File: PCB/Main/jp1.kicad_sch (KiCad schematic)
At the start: 1 part, among them U1 ORANGE_PI_CM4

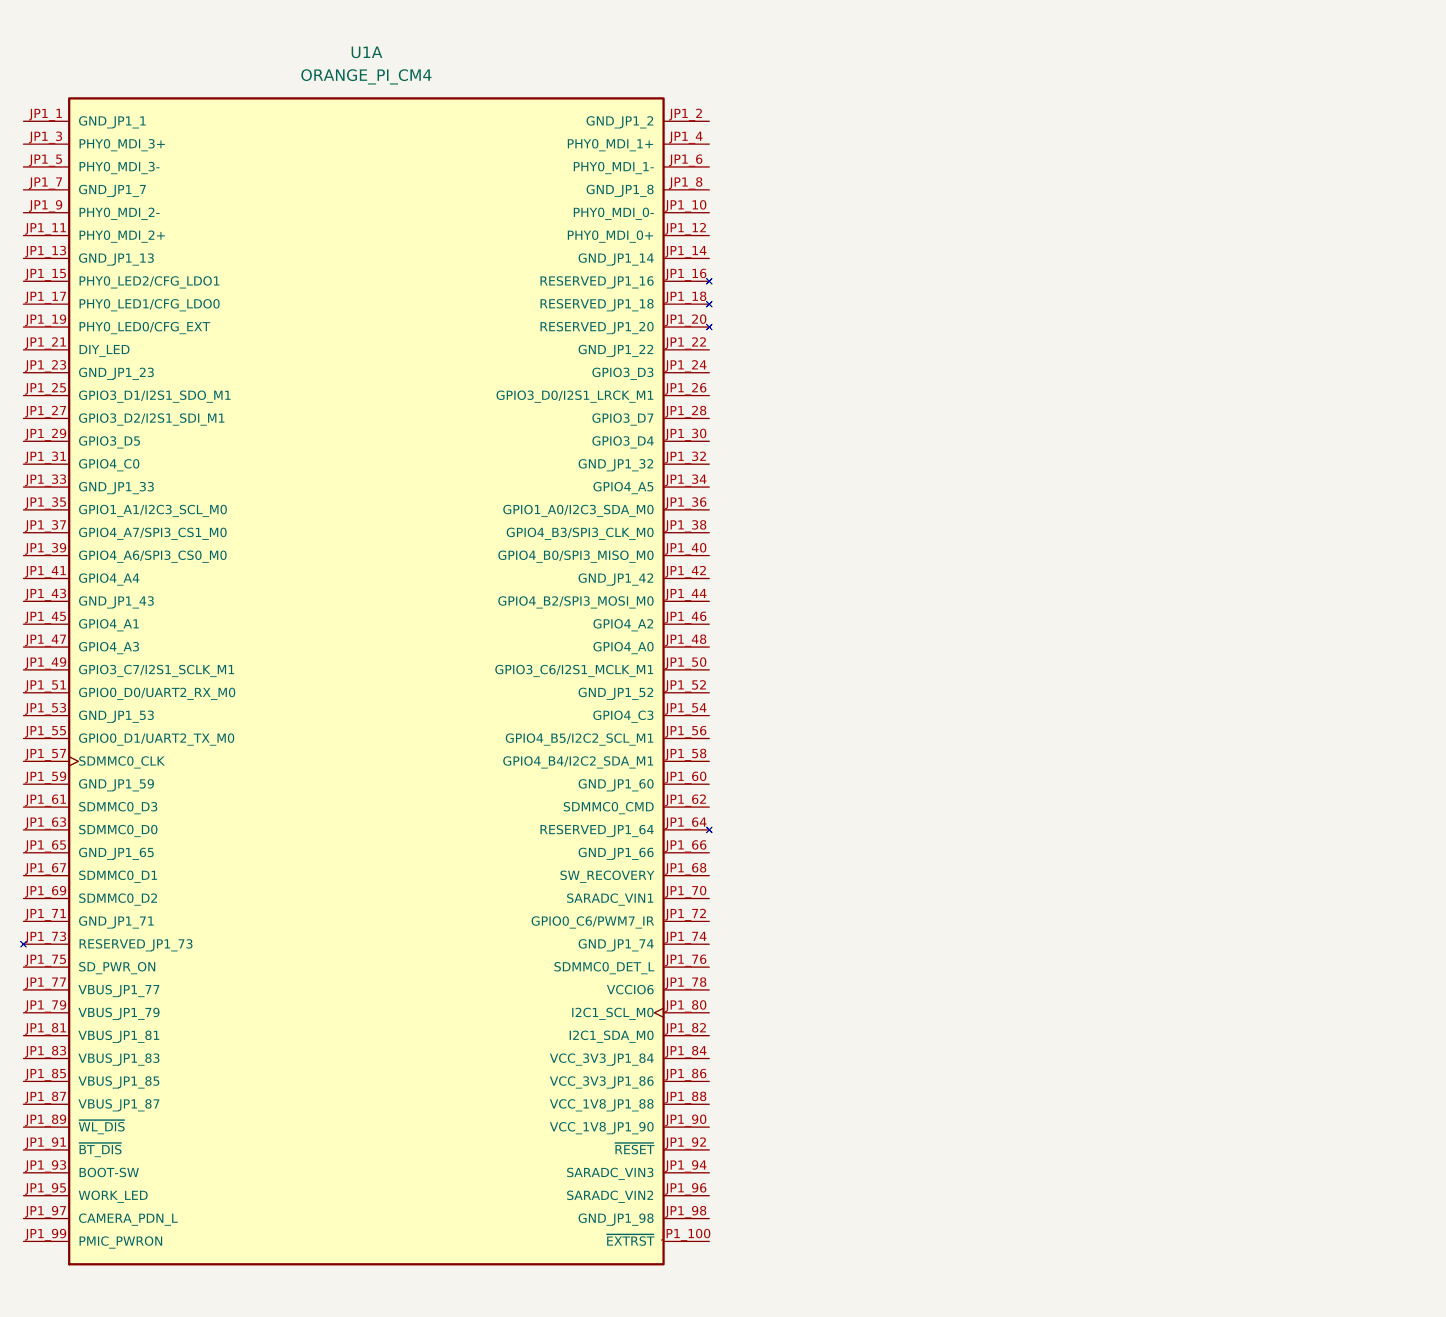
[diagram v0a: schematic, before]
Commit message: renaming y basico sin pcb
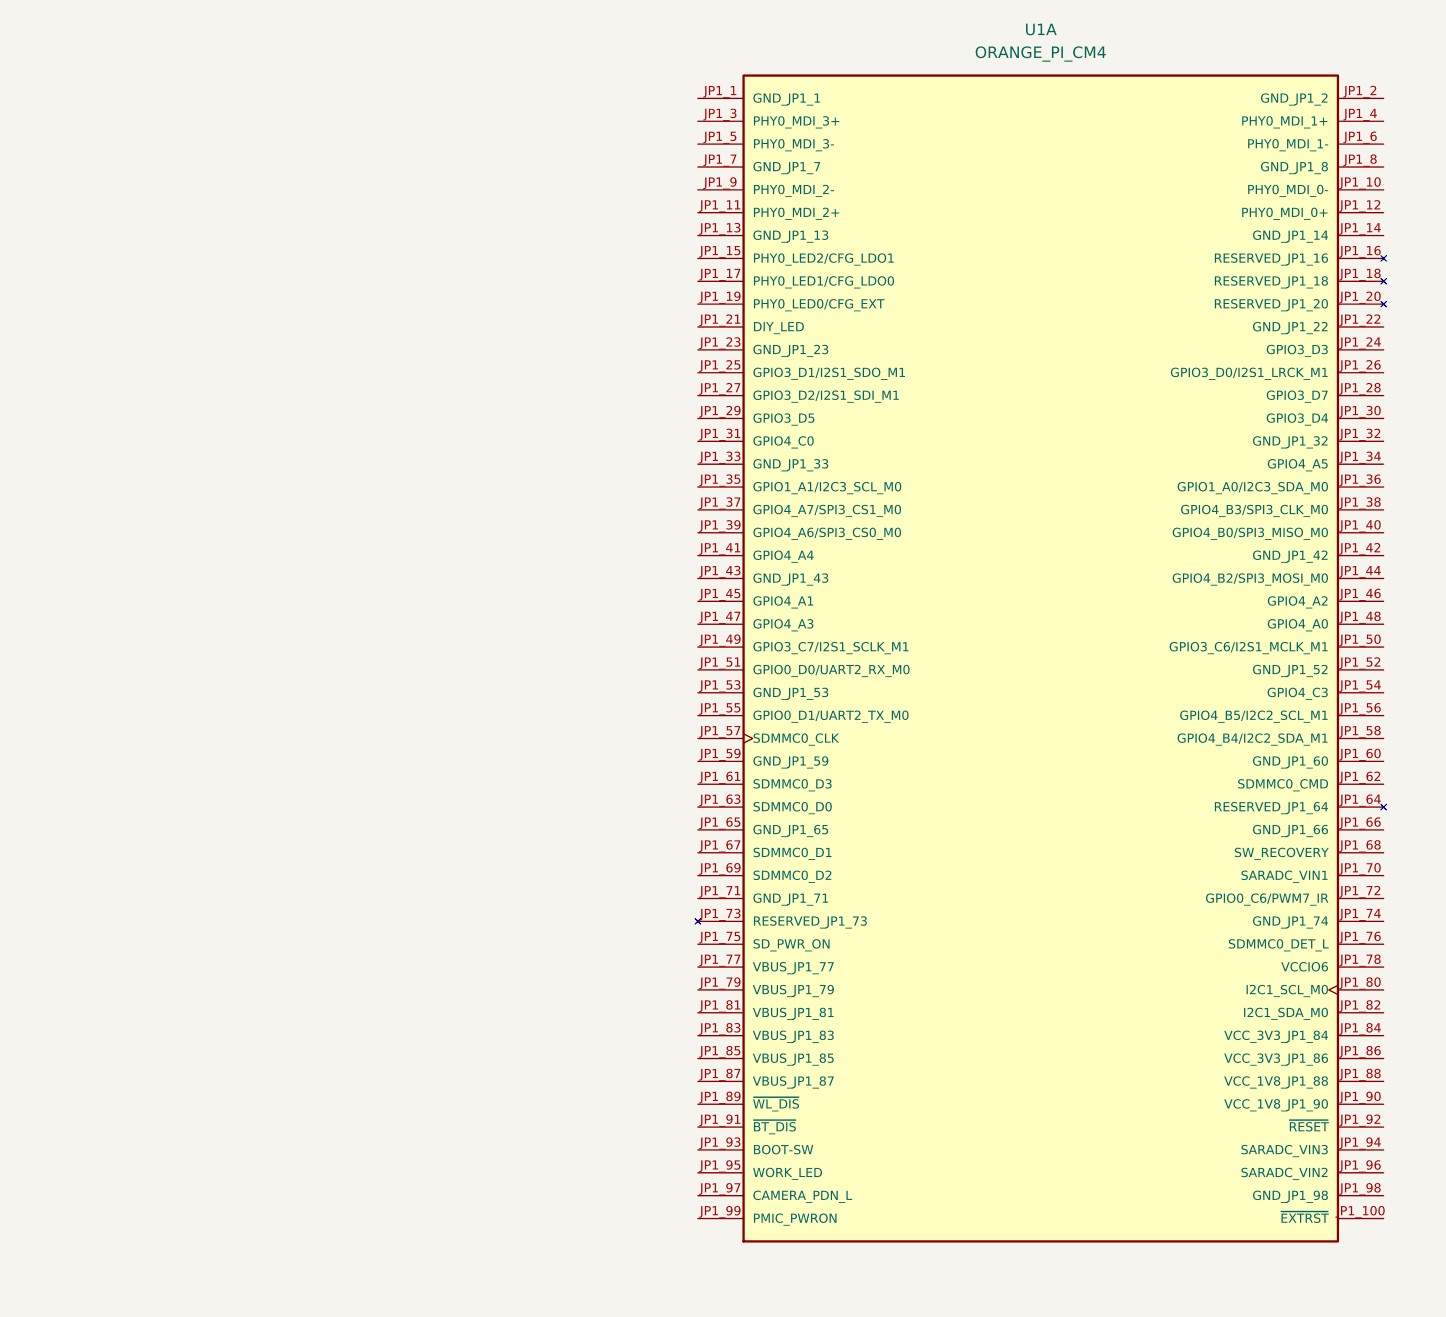
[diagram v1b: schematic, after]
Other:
- moved on the sheet: U1A
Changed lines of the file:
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@@
 	(symbol
 		(lib_id "OCM4:ORANGE_PI_CM4")
-		(at 156.21 96.52 0)
+		(at 231.14 93.98 0)
 		(unit 1)
 		(exclude_from_sim no)
@@
 		(fields_autoplaced yes)
 		(property "Reference" "U1"
-			(at 156.21 25.4 0)
+			(at 231.14 22.86 0)
 			(effects
 				(font
@@
 		)
 		(property "Value" "ORANGE_PI_CM4"
-			(at 156.21 27.94 0)
+			(at 231.14 25.4 0)
 			(effects
 				(font
@@
 		)
 		(property "Footprint" "Footprint:OCM4"
-			(at 156.21 96.52 0)
+			(at 231.14 93.98 0)
 			(effects
 				(font
@@
 		)
 		(property "Datasheet" ""
-			(at 156.21 96.52 0)
+			(at 231.14 93.98 0)
 			(effects
 				(font
@@
 		)
 		(property "Description" ""
-			(at 156.21 96.52 0)
+			(at 231.14 93.98 0)
 			(effects
 				(font
@@
 		)
 		(property "MF" "Orange Pi"
-			(at 156.21 96.52 0)
+			(at 231.14 93.98 0)
 			(effects
 				(font
@@
 		)
 		(property "MAXIMUM_PACKAGE_HEIGHT" "5.1mm"
-			(at 156.21 96.52 0)
+			(at 231.14 93.98 0)
 			(effects
 				(font
@@
 		)
 		(property "Package" "Package"
-			(at 156.21 96.52 0)
+			(at 231.14 93.98 0)
 			(effects
 				(font
@@
 		)
 		(property "Price" "None"
-			(at 156.21 96.52 0)
+			(at 231.14 93.98 0)
 			(effects
 				(font
@@
 		)
 		(property "Check_prices" "https://www.snapeda.com/parts/Orange%20Pi%20CM4/Orange+Pi/view-part/?ref=eda"
-			(at 156.21 96.52 0)
+			(at 231.14 93.98 0)
 			(effects
 				(font
@@
 		)
 		(property "STANDARD" "Manufacturer Recommendations"
-			(at 156.21 96.52 0)
+			(at 231.14 93.98 0)
 			(effects
 				(font
@@
 		)
 		(property "PARTREV" "v1.2"
-			(at 156.21 96.52 0)
+			(at 231.14 93.98 0)
 			(effects
 				(font
@@
 		)
 		(property "SnapEDA_Link" "https://www.snapeda.com/parts/Orange%20Pi%20CM4/Orange+Pi/view-part/?ref=snap"
-			(at 156.21 96.52 0)
+			(at 231.14 93.98 0)
 			(effects
 				(font
@@
 		)
 		(property "MP" "Orange Pi CM4"
-			(at 156.21 96.52 0)
+			(at 231.14 93.98 0)
 			(effects
 				(font
@@
 		)
 		(property "Description_1" "Orange Pi Compute Module 4"
-			(at 156.21 96.52 0)
+			(at 231.14 93.98 0)
 			(effects
 				(font
@@
 		)
 		(property "Availability" "Not in stock"
-			(at 156.21 96.52 0)
+			(at 231.14 93.98 0)
 			(effects
 				(font
@@
 		)
 		(property "MANUFACTURER" "Orange Pi"
-			(at 156.21 96.52 0)
+			(at 231.14 93.98 0)
 			(effects
 				(font

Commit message: pcb continued
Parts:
- added C2: 100nF, Capacitor_SMD:C_0603_1608Metric, symbol Device:C
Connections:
- net GND: now reaches U1.JP1_1 (GND_JP1_1)
- net GND: now also U1.JP1_13 (GND_JP1_13), U1.JP1_14 (GND_JP1_14), U1.JP1_2 (GND_JP1_2), U1.JP1_22 (GND_JP1_22), U1.JP1_23 (GND_JP1_23), U1.JP1_32 (GND_JP1_32), U1.JP1_33 (GND_JP1_33), U1.JP1_42 (GND_JP1_42), U1.JP1_43 (GND_JP1_43), U1.JP1_52 (GND_JP1_52), U1.JP1_53 (GND_JP1_53), U1.JP1_59 (GND_JP1_59), U1.JP1_60 (GND_JP1_60), U1.JP1_65 (GND_JP1_65), U1.JP1_66 (GND_JP1_66), U1.JP1_7 (GND_JP1_7), U1.JP1_71 (GND_JP1_71), U1.JP1_74 (GND_JP1_74), U1.JP1_8 (GND_JP1_8), U1.JP1_98 (GND_JP1_98)
- net +5V: now reaches U1.JP1_77 (VBUS_JP1_77)
- net +5V: now also U1.JP1_79 (VBUS_JP1_79), U1.JP1_81 (VBUS_JP1_81), U1.JP1_83 (VBUS_JP1_83), U1.JP1_85 (VBUS_JP1_85), U1.JP1_87 (VBUS_JP1_87)
- net EN: now reaches U1.JP1_99 (PMIC_PWRON)
